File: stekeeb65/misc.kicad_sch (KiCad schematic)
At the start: 7 parts

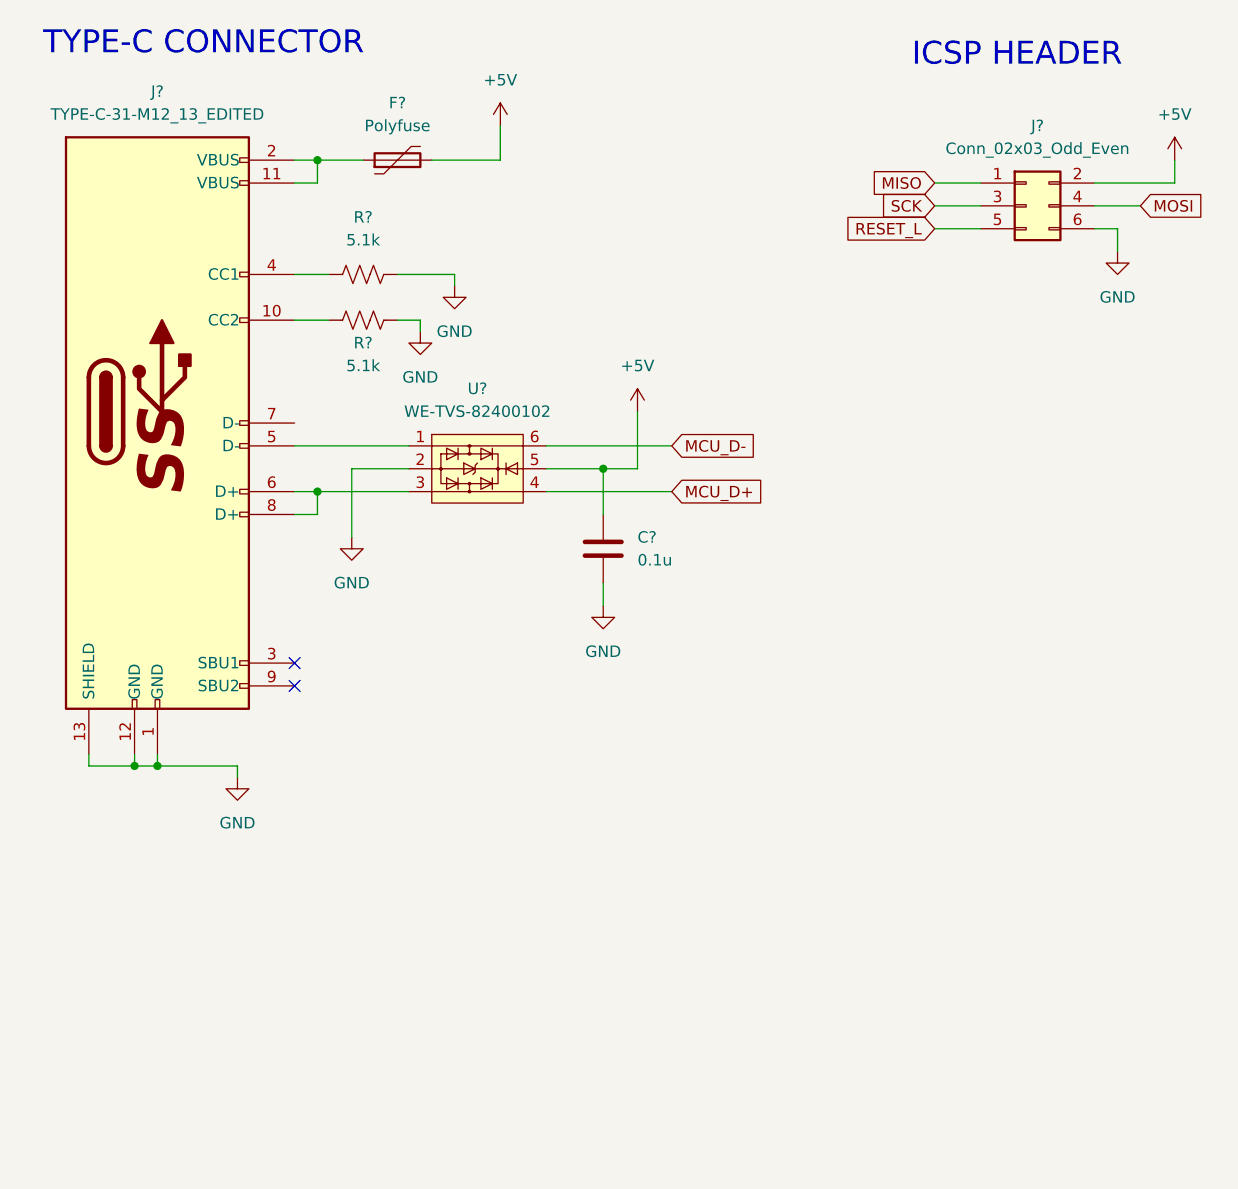
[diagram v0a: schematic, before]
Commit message: Adding keyboard footprints
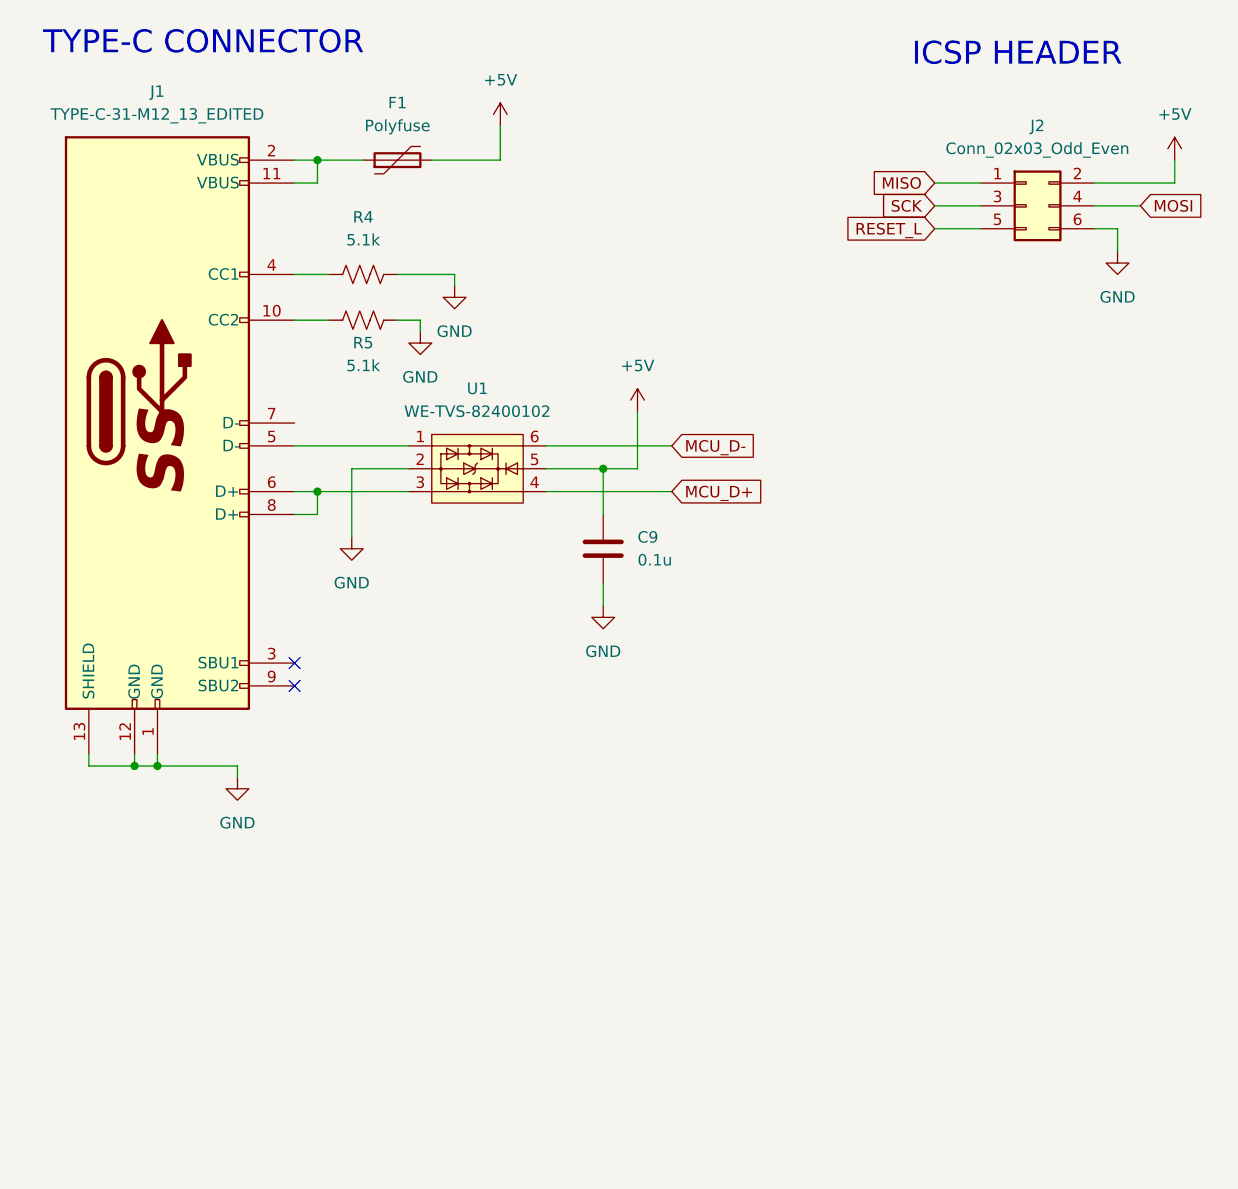
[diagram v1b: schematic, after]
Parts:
- C9: renamed from C?; footprint (none) -> Capacitor_SMD:C_0805_2012Metric_Pad1.18x1.45mm_HandSolder
- F1: renamed from F?; footprint (none) -> Fuse:Fuse_0805_2012Metric_Pad1.15x1.40mm_HandSolder
- J2: renamed from J?; footprint (none) -> Connector_PinHeader_2.54mm:PinHeader_2x03_P2.54mm_Vertical
- R4, R5: renamed from R?; footprint (none) -> Resistor_SMD:R_0805_2012Metric_Pad1.20x1.40mm_HandSolder
- gave numbers to parts that had none: 2
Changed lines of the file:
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@@
   (symbol (lib_id "power:GND") (at 88.9 83.82 0) (unit 1)
     (in_bom yes) (on_board yes) (fields_autoplaced)
-    (property "Reference" "#PWR?" (id 0) (at 88.9 90.17 0)
+    (property "Reference" "#PWR020" (id 0) (at 88.9 90.17 0)
       (effects (font (size 1.27 1.27)) hide)
     )
@@
   (symbol (lib_id "Device:C") (at 88.9 77.47 0) (unit 1)
     (in_bom yes) (on_board yes) (fields_autoplaced)
-    (property "Reference" "C?" (id 0) (at 92.71 76.1999 0)
+    (property "Reference" "C9" (id 0) (at 92.71 76.1999 0)
       (effects (font (size 1.27 1.27)) (justify left))
     )
@@
       (effects (font (size 1.27 1.27)) (justify left))
     )
-    (property "Footprint" "" (id 2) (at 89.8652 81.28 0)
+    (property "Footprint" "Capacitor_SMD:C_0805_2012Metric_Pad1.18x1.45mm_HandSolder" (id 2) (at 89.8652 81.28 0)
       (effects (font (size 1.27 1.27)) hide)
     )
@@
   (symbol (lib_id "mini_random_library:TYPE-C-31-M12_13_EDITED") (at 39.37 63.5 0) (unit 1)
     (in_bom yes) (on_board yes) (fields_autoplaced)
-    (property "Reference" "J?" (id 0) (at 39.37 26.67 0))
+    (property "Reference" "J1" (id 0) (at 39.37 26.67 0))
     (property "Value" "TYPE-C-31-M12_13_EDITED" (id 1) (at 39.37 29.21 0))
     (property "Footprint" "acheronConnectors:TYPE-C-31-M-12" (id 2) (at 26.67 62.23 90)
@@
   (symbol (lib_id "power:GND") (at 60.96 76.2 0) (unit 1)
     (in_bom yes) (on_board yes) (fields_autoplaced)
-    (property "Reference" "#PWR?" (id 0) (at 60.96 82.55 0)
+    (property "Reference" "#PWR016" (id 0) (at 60.96 82.55 0)
       (effects (font (size 1.27 1.27)) hide)
     )
@@
   (symbol (lib_id "power:GND") (at 72.39 48.26 0) (unit 1)
     (in_bom yes) (on_board yes) (fields_autoplaced)
-    (property "Reference" "#PWR?" (id 0) (at 72.39 54.61 0)
+    (property "Reference" "#PWR018" (id 0) (at 72.39 54.61 0)
       (effects (font (size 1.27 1.27)) hide)
     )
@@
   (symbol (lib_id "Device:R_US") (at 62.23 46.99 90) (unit 1)
     (in_bom yes) (on_board yes) (fields_autoplaced)
-    (property "Reference" "R?" (id 0) (at 62.23 40.64 90))
+    (property "Reference" "R4" (id 0) (at 62.23 40.64 90))
     (property "Value" "5.1k" (id 1) (at 62.23 43.18 90))
-    (property "Footprint" "" (id 2) (at 62.484 45.974 90)
+    (property "Footprint" "Resistor_SMD:R_0805_2012Metric_Pad1.20x1.40mm_HandSolder" (id 2) (at 62.484 45.974 90)
       (effects (font (size 1.27 1.27)) hide)
     )
@@
   (symbol (lib_id "power:+5V") (at 92.71 62.23 0) (unit 1)
     (in_bom yes) (on_board yes) (fields_autoplaced)
-    (property "Reference" "#PWR?" (id 0) (at 92.71 66.04 0)
+    (property "Reference" "#PWR021" (id 0) (at 92.71 66.04 0)
       (effects (font (size 1.27 1.27)) hide)
     )
@@
   (symbol (lib_id "Device:R_US") (at 62.23 52.07 90) (unit 1)
     (in_bom yes) (on_board yes)
-    (property "Reference" "R?" (id 0) (at 62.23 54.61 90))
+    (property "Reference" "R5" (id 0) (at 62.23 54.61 90))
     (property "Value" "5.1k" (id 1) (at 62.23 57.15 90))
-    (property "Footprint" "" (id 2) (at 62.484 51.054 90)
+    (property "Footprint" "Resistor_SMD:R_0805_2012Metric_Pad1.20x1.40mm_HandSolder" (id 2) (at 62.484 51.054 90)
       (effects (font (size 1.27 1.27)) hide)
     )
@@
   (symbol (lib_id "power:GND") (at 146.05 44.45 0) (unit 1)
     (in_bom yes) (on_board yes) (fields_autoplaced)
-    (property "Reference" "#PWR?" (id 0) (at 146.05 50.8 0)
+    (property "Reference" "#PWR022" (id 0) (at 146.05 50.8 0)
       (effects (font (size 1.27 1.27)) hide)
     )
@@
   (symbol (lib_id "power:GND") (at 48.26 102.87 0) (unit 1)
     (in_bom yes) (on_board yes) (fields_autoplaced)
-    (property "Reference" "#PWR?" (id 0) (at 48.26 109.22 0)
+    (property "Reference" "#PWR015" (id 0) (at 48.26 109.22 0)
       (effects (font (size 1.27 1.27)) hide)
     )
@@
   (symbol (lib_id "power:+5V") (at 77.47 30.48 0) (unit 1)
     (in_bom yes) (on_board yes) (fields_autoplaced)
-    (property "Reference" "#PWR?" (id 0) (at 77.47 34.29 0)
+    (property "Reference" "#PWR019" (id 0) (at 77.47 34.29 0)
       (effects (font (size 1.27 1.27)) hide)
     )
@@
   (symbol (lib_id "power:+5V") (at 152.4 34.29 0) (unit 1)
     (in_bom yes) (on_board yes) (fields_autoplaced)
-    (property "Reference" "#PWR?" (id 0) (at 152.4 38.1 0)
+    (property "Reference" "#PWR023" (id 0) (at 152.4 38.1 0)
       (effects (font (size 1.27 1.27)) hide)
     )
@@
   (symbol (lib_id "Power_Protection:WE-TVS-82400102") (at 74.93 68.58 0) (unit 1)
     (in_bom yes) (on_board yes) (fields_autoplaced)
-    (property "Reference" "U?" (id 0) (at 74.93 59.69 0))
+    (property "Reference" "U1" (id 0) (at 74.93 59.69 0))
     (property "Value" "WE-TVS-82400102" (id 1) (at 74.93 62.23 0))
     (property "Footprint" "Package_TO_SOT_SMD:SOT-23-6" (id 2) (at 74.93 73.66 0)
@@
   (symbol (lib_id "power:GND") (at 68.58 53.34 0) (unit 1)
     (in_bom yes) (on_board yes) (fields_autoplaced)
-    (property "Reference" "#PWR?" (id 0) (at 68.58 59.69 0)
+    (property "Reference" "#PWR017" (id 0) (at 68.58 59.69 0)
       (effects (font (size 1.27 1.27)) hide)
     )
@@
   (symbol (lib_id "Connector_Generic:Conn_02x03_Odd_Even") (at 135.89 39.37 0) (unit 1)
     (in_bom yes) (on_board yes) (fields_autoplaced)
-    (property "Reference" "J?" (id 0) (at 137.16 30.48 0))
+    (property "Reference" "J2" (id 0) (at 137.16 30.48 0))
     (property "Value" "Conn_02x03_Odd_Even" (id 1) (at 137.16 33.02 0))
-    (property "Footprint" "" (id 2) (at 135.89 39.37 0)
+    (property "Footprint" "Connector_PinHeader_2.54mm:PinHeader_2x03_P2.54mm_Vertical" (id 2) (at 135.89 39.37 0)
       (effects (font (size 1.27 1.27)) hide)
     )
@@
   (symbol (lib_id "Device:Polyfuse") (at 66.04 34.29 90) (unit 1)
     (in_bom yes) (on_board yes) (fields_autoplaced)
-    (property "Reference" "F?" (id 0) (at 66.04 27.94 90))
+    (property "Reference" "F1" (id 0) (at 66.04 27.94 90))
     (property "Value" "Polyfuse" (id 1) (at 66.04 30.48 90))
-    (property "Footprint" "" (id 2) (at 71.12 33.02 0)
+    (property "Footprint" "Fuse:Fuse_0805_2012Metric_Pad1.15x1.40mm_HandSolder" (id 2) (at 71.12 33.02 0)
       (effects (font (size 1.27 1.27)) (justify left) hide)
     )

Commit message: Committing before changes to PCB
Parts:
- J1: footprint acheronConnectors:TYPE-C-31-M-12 -> Type-C:HRO-TYPE-C-31-M-12-HandSoldering
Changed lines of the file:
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@@
     (property "Reference" "J1" (id 0) (at 39.37 26.67 0))
     (property "Value" "TYPE-C-31-M12_13_EDITED" (id 1) (at 39.37 29.21 0))
-    (property "Footprint" "acheronConnectors:TYPE-C-31-M-12" (id 2) (at 26.67 62.23 90)
+    (property "Footprint" "Type-C:HRO-TYPE-C-31-M-12-HandSoldering" (id 2) (at 26.67 62.23 90)
       (effects (font (size 1.27 1.27)) hide)
     )
